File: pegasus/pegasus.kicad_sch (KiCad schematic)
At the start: 11 parts, among them IC1 L7805ACV, IC2 RFD900, IC3 L70B-M39, U1 Teensy4.0, U2 CON-SMA-EDGE-S, U3 CON-SMA-EDGE-S

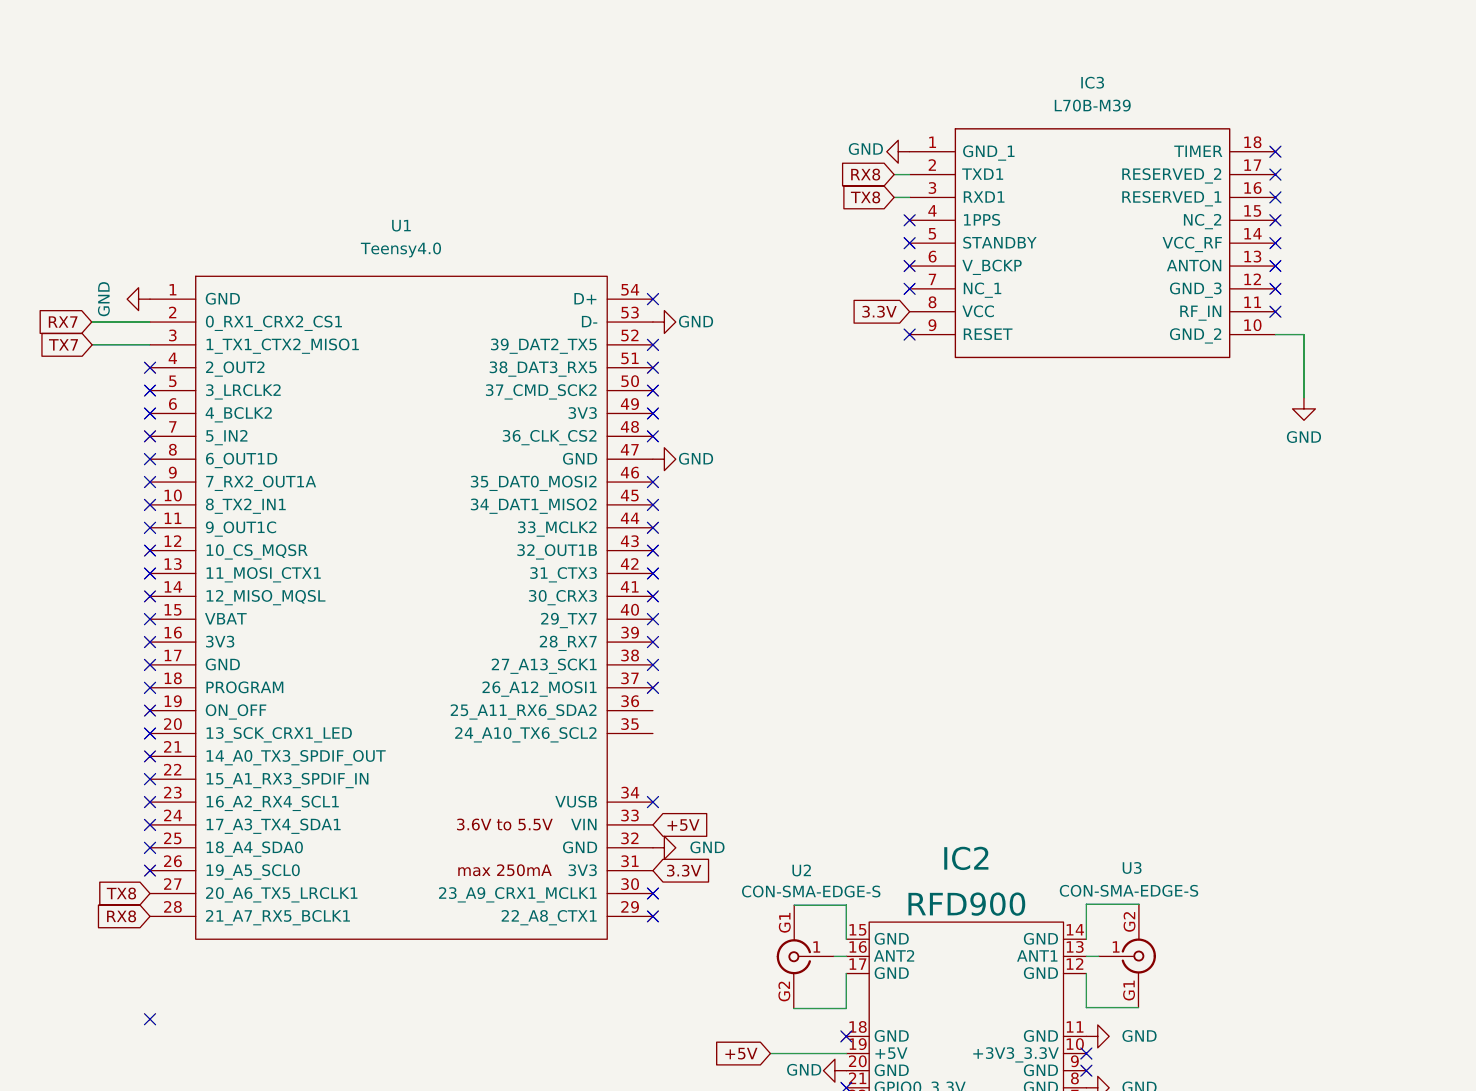
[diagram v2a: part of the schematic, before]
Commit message: add external RX TX connectors
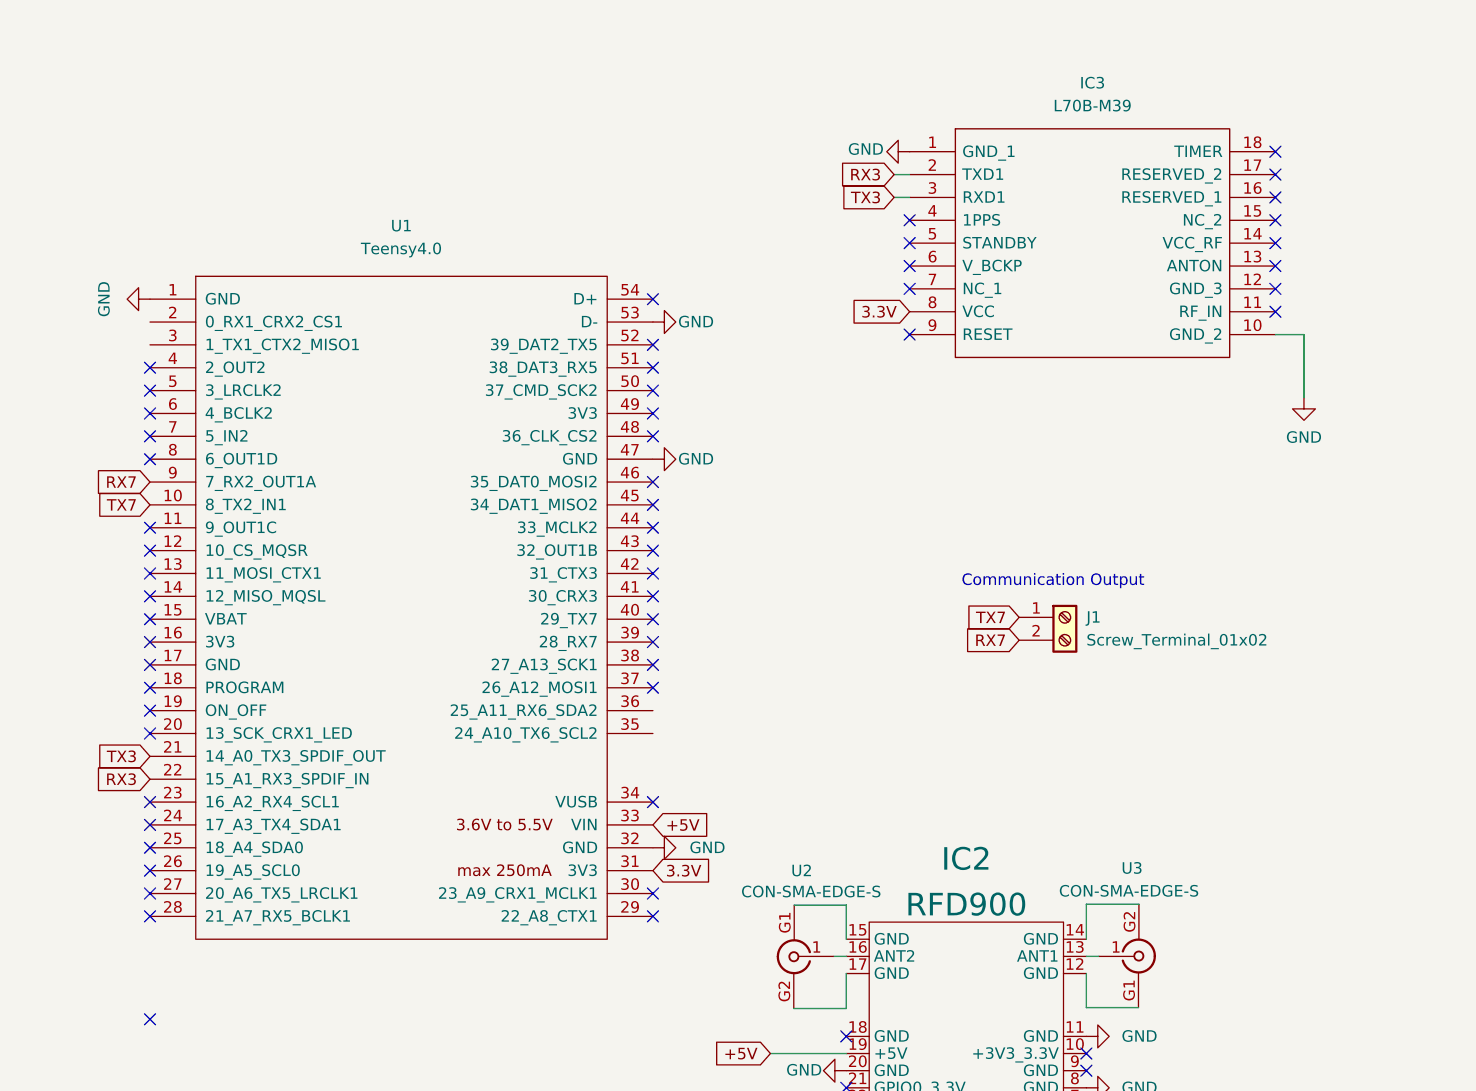
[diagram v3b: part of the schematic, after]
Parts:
- added J1: Screw_Terminal_01x02, RS-Components:SHDR2W105P0X500_1X2_1060X900X1250P, symbol Connector:Screw_Terminal_01x02
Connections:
- net RX7: now also U1.9 (7_RX2_OUT1A), J1.2 (Pin_2); no longer U1.2 (0_RX1_CRX2_CS1)
- net TX7: now also U1.10 (8_TX2_IN1), J1.1 (Pin_1); no longer U1.3 (1_TX1_CTX2_MISO1)
- net TX3: now reaches U1.21 (14_A0_TX3_SPDIF_OUT)
- net TX3: now also IC3.3 (RXD1)
- net RX3: now reaches U1.22 (15_A1_RX3_SPDIF_IN)
- net RX3: now also IC3.2 (TXD1)
- net RX8: no longer names the net of U1.28 (21_A7_RX5_BCLK1)
- net RX8: no longer IC3.2 (TXD1)
- net TX8: no longer names the net of U1.27 (20_A6_TX5_LRCLK1)
- net TX8: no longer IC3.3 (RXD1)
- no-connect marks 72 -> 70
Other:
- note added: "Communication Output"
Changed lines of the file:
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@@
   (no_connect (at 41.91 109.22))
   (no_connect (at 41.91 104.14))
-  (no_connect (at 41.91 111.76))
   (no_connect (at 41.91 106.68))
   (no_connect (at 41.91 101.6))
   (no_connect (at 41.91 99.06))
-  (no_connect (at 41.91 114.3))
   (no_connect (at 41.91 121.92))
   (no_connect (at 41.91 119.38))
@@
   (no_connect (at 41.91 139.7))
   (no_connect (at 41.91 171.45))
-  (no_connect (at 41.91 142.24))
+  (no_connect (at 41.91 147.32))
   (no_connect (at 41.91 154.94))
   (no_connect (at 41.91 149.86))
-  (no_connect (at 41.91 147.32))
-  (no_connect (at 41.91 144.78))
+  (no_connect (at 41.91 160.02))
+  (no_connect (at 41.91 157.48))
   (no_connect (at 145.9484 186.69))
   (no_connect (at 119.2784 192.405))
@@
     (stroke (width 0) (type default) (color 0 0 0 0))
   )
-  (wire (pts (xy 35.433 93.98) (xy 41.91 93.98))
-    (stroke (width 0) (type default) (color 0 0 0 0))
-  )
   (wire (pts (xy 56.134 34.544) (xy 56.134 42.164))
     (stroke (width 0) (type default) (color 0 0 0 0))
@@
     (stroke (width 0) (type default) (color 0 0 0 0))
   )
-  (wire (pts (xy 35.4838 96.52) (xy 41.91 96.52))
-    (stroke (width 0) (type default) (color 0 0 0 0))
-  )
   (wire (pts (xy 117.6528 188.595) (xy 119.2784 188.595))
     (stroke (width 0) (type default) (color 0 0 0 0))
@@
   (wire (pts (xy 145.9484 170.1546) (xy 145.9484 166.37))
     (stroke (width 0) (type default) (color 0 0 0 0))
+  )
+  (text "Communication Output\n" (at 132.08 123.5964 0)
+    (effects (font (size 1.27 1.27)) (justify left bottom))
   )
   (text "Switch\n" (at 38.1 37.846 90)
@@
     )
   )
-  (global_label "RX7" (shape input) (at 35.433 93.98 180) (fields_autoplaced)
-    (effects (font (size 1.27 1.27)) (justify right))
-    (property "Intersheet References" "${INTERSHEET_REFS}" (id 0) (at 29.3309 93.9006 0)
+  (global_label "RX7" (shape input) (at 41.91 111.76 180) (fields_autoplaced)
+    (effects (font (size 1.27 1.27)) (justify right))
+    (property "Intersheet References" "${INTERSHEET_REFS}" (id 0) (at 35.8079 111.6806 0)
       (effects (font (size 1.27 1.27)) (justify right) hide)
     )
@@
     )
   )
-  (global_label "RX8" (shape input) (at 41.91 160.02 180) (fields_autoplaced)
-    (effects (font (size 1.27 1.27)) (justify right))
-    (property "Intersheet References" "${INTERSHEET_REFS}" (id 0) (at 35.8079 160.0994 0)
+  (global_label "RX3" (shape input) (at 41.91 144.78 180) (fields_autoplaced)
+    (effects (font (size 1.27 1.27)) (justify right))
+    (property "Intersheet References" "${INTERSHEET_REFS}" (id 0) (at 35.8079 144.7006 0)
       (effects (font (size 1.27 1.27)) (justify right) hide)
     )
@@
     )
   )
-  (global_label "RX8" (shape input) (at 124.587 77.597 180) (fields_autoplaced)
-    (effects (font (size 1.27 1.27)) (justify right))
-    (property "Intersheet References" "${INTERSHEET_REFS}" (id 0) (at 118.4849 77.6764 0)
-      (effects (font (size 1.27 1.27)) (justify right) hide)
-    )
-  )
-  (global_label "TX8" (shape input) (at 124.587 80.137 180) (fields_autoplaced)
-    (effects (font (size 1.27 1.27)) (justify right))
-    (property "Intersheet References" "${INTERSHEET_REFS}" (id 0) (at 118.7872 80.2164 0)
+  (global_label "RX3" (shape input) (at 124.587 77.597 180) (fields_autoplaced)
+    (effects (font (size 1.27 1.27)) (justify right))
+    (property "Intersheet References" "${INTERSHEET_REFS}" (id 0) (at 118.4849 77.5176 0)
+      (effects (font (size 1.27 1.27)) (justify right) hide)
+    )
+  )
+  (global_label "TX3" (shape input) (at 124.587 80.137 180) (fields_autoplaced)
+    (effects (font (size 1.27 1.27)) (justify right))
+    (property "Intersheet References" "${INTERSHEET_REFS}" (id 0) (at 118.7872 80.0576 0)
+      (effects (font (size 1.27 1.27)) (justify right) hide)
+    )
+  )
+  (global_label "TX7" (shape input) (at 138.4808 126.7968 180) (fields_autoplaced)
+    (effects (font (size 1.27 1.27)) (justify right))
+    (property "Intersheet References" "${INTERSHEET_REFS}" (id 0) (at 132.681 126.7174 0)
       (effects (font (size 1.27 1.27)) (justify right) hide)
     )
@@
     )
   )
-  (global_label "TX8" (shape input) (at 41.91 157.48 180) (fields_autoplaced)
-    (effects (font (size 1.27 1.27)) (justify right))
-    (property "Intersheet References" "${INTERSHEET_REFS}" (id 0) (at 36.1102 157.5594 0)
+  (global_label "TX3" (shape input) (at 41.91 142.24 180) (fields_autoplaced)
+    (effects (font (size 1.27 1.27)) (justify right))
+    (property "Intersheet References" "${INTERSHEET_REFS}" (id 0) (at 36.1102 142.1606 0)
       (effects (font (size 1.27 1.27)) (justify right) hide)
     )
@@
     )
   )
-  (global_label "TX7" (shape input) (at 35.4838 96.52 180) (fields_autoplaced)
-    (effects (font (size 1.27 1.27)) (justify right))
-    (property "Intersheet References" "${INTERSHEET_REFS}" (id 0) (at 29.684 96.4406 0)
+  (global_label "RX7" (shape input) (at 138.4808 129.3368 180) (fields_autoplaced)
+    (effects (font (size 1.27 1.27)) (justify right))
+    (property "Intersheet References" "${INTERSHEET_REFS}" (id 0) (at 132.3787 129.2574 0)
+      (effects (font (size 1.27 1.27)) (justify right) hide)
+    )
+  )
+  (global_label "TX7" (shape input) (at 41.91 114.3 180) (fields_autoplaced)
+    (effects (font (size 1.27 1.27)) (justify right))
+    (property "Intersheet References" "${INTERSHEET_REFS}" (id 0) (at 36.1102 114.2206 0)
       (effects (font (size 1.27 1.27)) (justify right) hide)
     )
@@
   (symbol (lib_id "power:GND") (at 196.342 25.4 0) (unit 1)
     (in_bom yes) (on_board yes) (fields_autoplaced)
-    (property "Reference" "#PWR012" (id 0) (at 196.342 31.75 0)
+    (property "Reference" "#PWR011" (id 0) (at 196.342 31.75 0)
       (effects (font (size 1.27 1.27)) hide)
     )
@@
   (symbol (lib_id "power:GND") (at 214.376 25.908 0) (unit 1)
     (in_bom yes) (on_board yes) (fields_autoplaced)
-    (property "Reference" "#PWR013" (id 0) (at 214.376 32.258 0)
+    (property "Reference" "#PWR012" (id 0) (at 214.376 32.258 0)
       (effects (font (size 1.27 1.27)) hide)
     )
@@
   (symbol (lib_id "power:GND") (at 250.698 25.908 0) (unit 1)
     (in_bom yes) (on_board yes) (fields_autoplaced)
-    (property "Reference" "#PWR016" (id 0) (at 250.698 32.258 0)
+    (property "Reference" "#PWR014" (id 0) (at 250.698 32.258 0)
       (effects (font (size 1.27 1.27)) hide)
     )
@@
     )
     (pin "1")
+  )
+  (symbol (lib_id "Connector:Screw_Terminal_01x02") (at 143.5608 126.7968 0) (unit 1)
+    (in_bom yes) (on_board yes) (fields_autoplaced)
+    (property "Reference" "J1" (id 0) (at 145.9484 126.7967 0)
+      (effects (font (size 1.27 1.27)) (justify left))
+    )
+    (property "Value" "Screw_Terminal_01x02" (id 1) (at 145.9484 129.3367 0)
+      (effects (font (size 1.27 1.27)) (justify left))
+    )
+    (property "Footprint" "RS-Components:SHDR2W105P0X500_1X2_1060X900X1250P" (id 2) (at 143.5608 126.7968 0)
+      (effects (font (size 1.27 1.27)) hide)
+    )
+    (property "Datasheet" "~" (id 3) (at 143.5608 126.7968 0)
+      (effects (font (size 1.27 1.27)) hide)
+    )
+    (pin "1")
+    (pin "2")
   )
   (symbol (lib_id "Quectel_L70B-M39:L70B-M39") (at 126.3142 75.057 0) (unit 1)
@@
   (symbol (lib_id "power:GND") (at 232.664 25.908 0) (unit 1)
     (in_bom yes) (on_board yes) (fields_autoplaced)
-    (property "Reference" "#PWR015" (id 0) (at 232.664 32.258 0)
+    (property "Reference" "#PWR013" (id 0) (at 232.664 32.258 0)
       (effects (font (size 1.27 1.27)) hide)
     )
@@
     )
     (path "/70e52f12-fb67-4276-ad30-28892fb20b86"
+      (reference "#PWR011") (unit 1) (value "GND") (footprint "")
+    )
+    (path "/78a4a849-1c24-4beb-98bb-5d8b5b1babf4"
       (reference "#PWR012") (unit 1) (value "GND") (footprint "")
     )
-    (path "/78a4a849-1c24-4beb-98bb-5d8b5b1babf4"
+    (path "/c629176b-abd3-4695-ae9b-e765a0bc8aed"
       (reference "#PWR013") (unit 1) (value "GND") (footprint "")
     )
-    (path "/c629176b-abd3-4695-ae9b-e765a0bc8aed"
-      (reference "#PWR015") (unit 1) (value "GND") (footprint "")
-    )
     (path "/abaa90e7-ead3-4e66-bb3e-cc1d7a6daa0e"
-      (reference "#PWR016") (unit 1) (value "GND") (footprint "")
+      (reference "#PWR014") (unit 1) (value "GND") (footprint "")
     )
     (path "/fa097515-aa33-445e-a81c-63a2092f37d7"
@@
       (reference "IC3") (unit 1) (value "L70B-M39") (footprint "Quectel_L70B-M39:1x18")
     )
+    (path "/bb9478d8-9393-4633-8eab-e3cdf1c5ff7e"
+      (reference "J1") (unit 1) (value "Screw_Terminal_01x02") (footprint "RS-Components:SHDR2W105P0X500_1X2_1060X900X1250P")
+    )
     (path "/d4822f5d-8c1d-4b0c-ba23-0826fc0572d8"

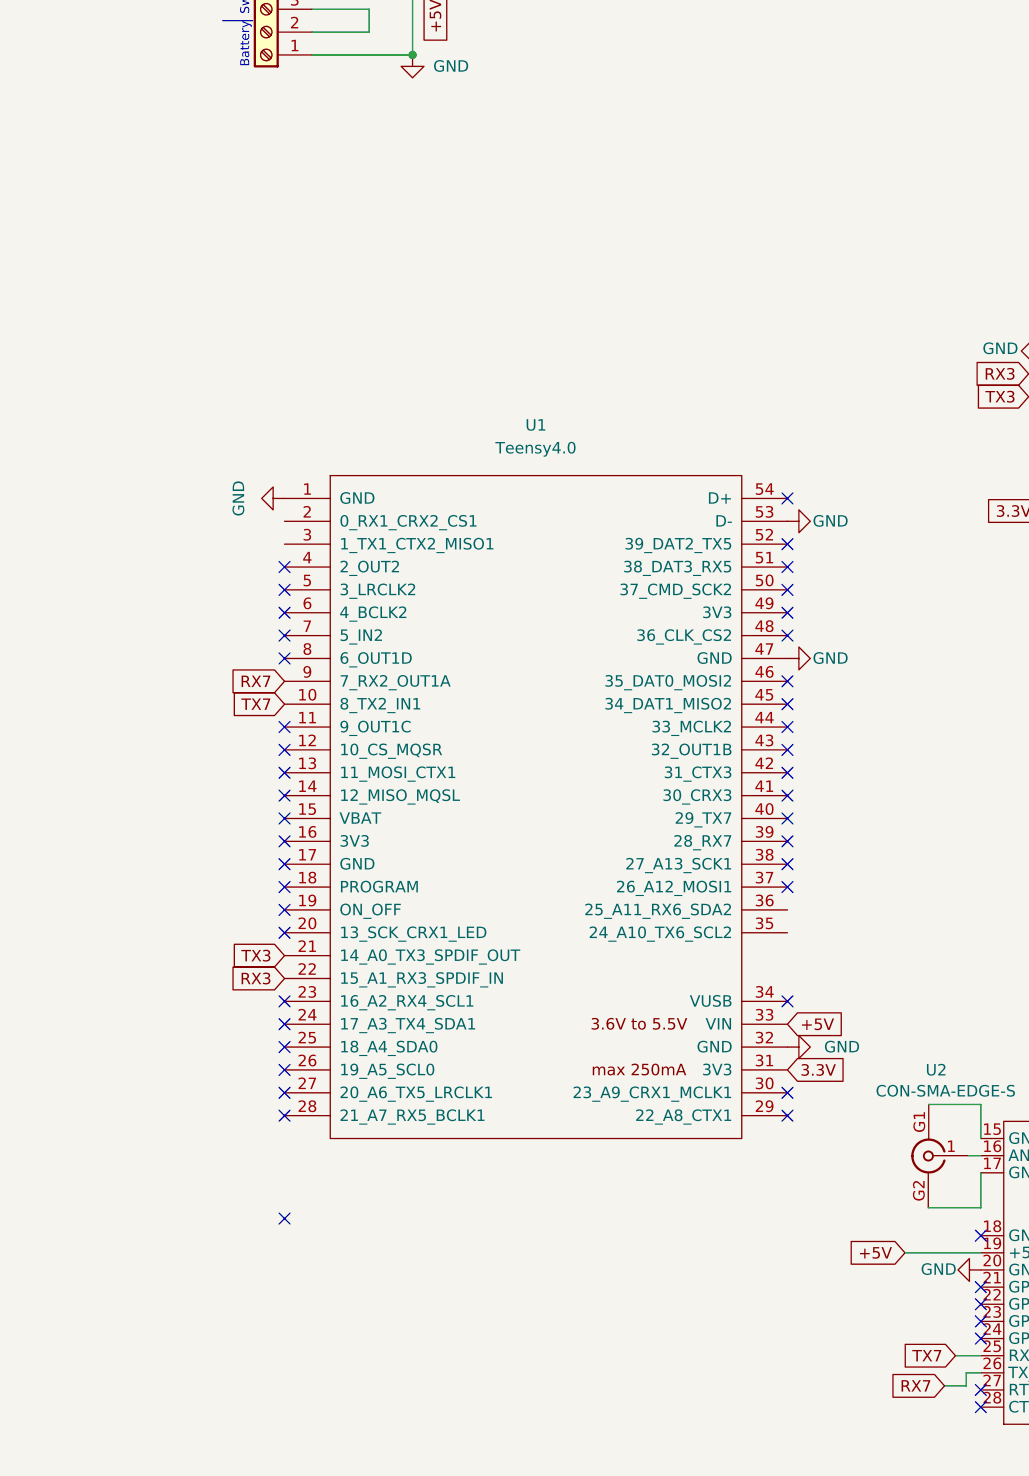
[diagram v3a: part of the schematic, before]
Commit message: add rgb led
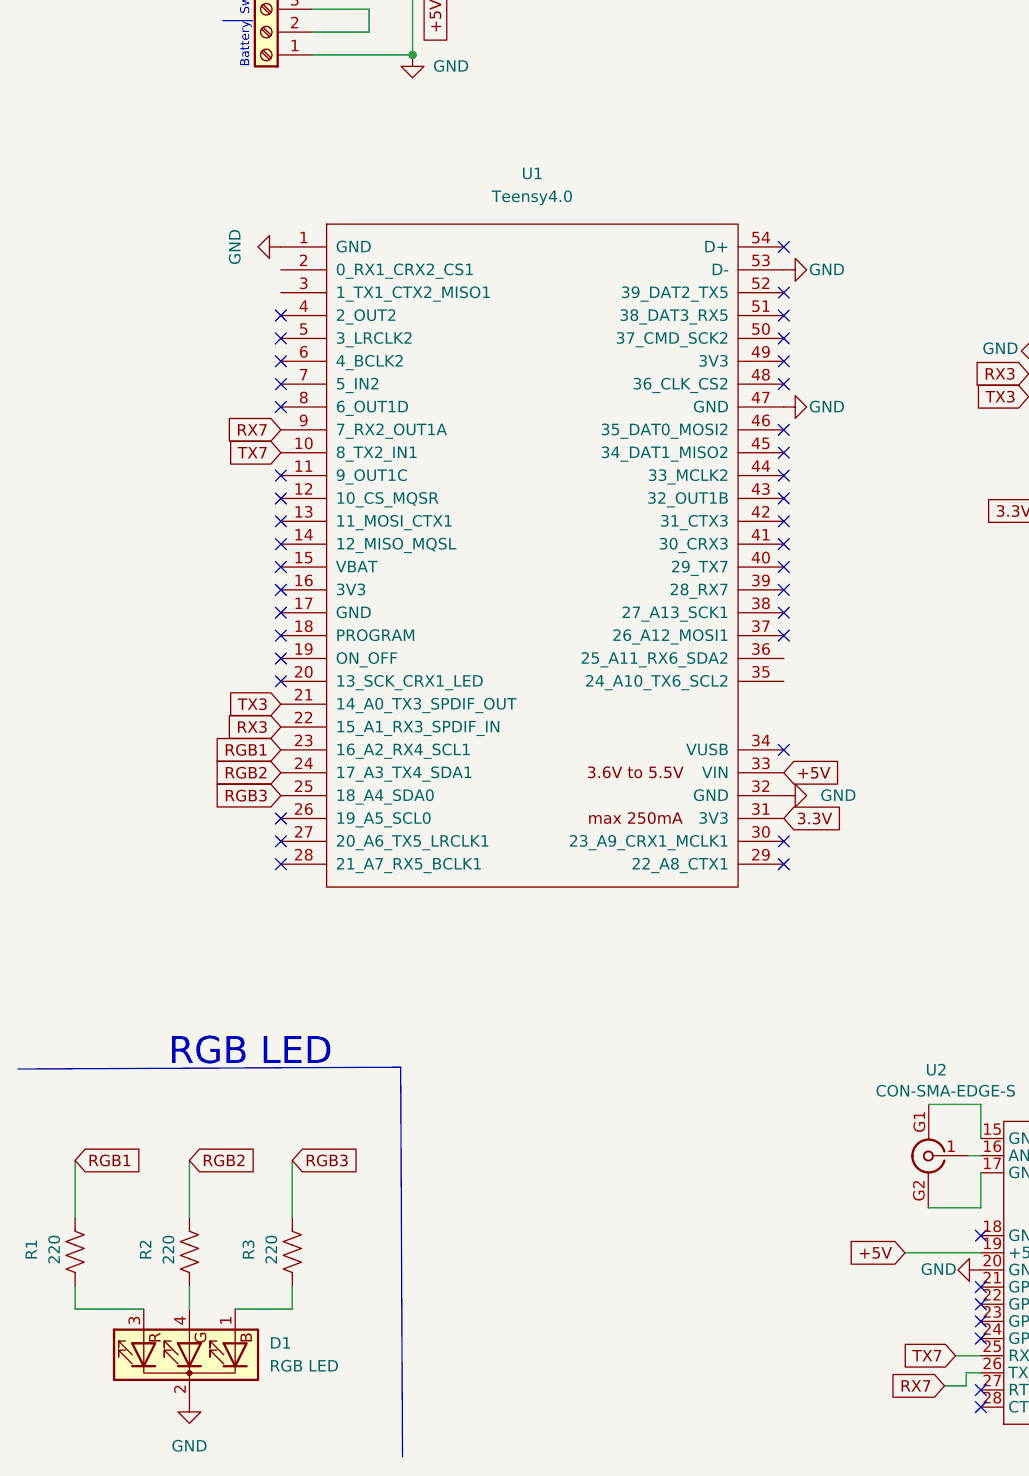
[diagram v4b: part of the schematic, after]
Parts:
- added D1: RGB LED, LED_THT:LED_D5.0mm-4_RGB, symbol Device:LED_BKRG
- added R1, R2, R3: 220, Resistor_SMD:R_1206_3216Metric_Pad1.30x1.75mm_HandSolder, symbol Device:R_US
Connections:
- net GND: now also D1.2 (K)
- net RGB1: now reaches U1.23 (16_A2_RX4_SCL1)
- net RGB1: now also R1.2
- net RGB2: now reaches U1.24 (17_A3_TX4_SDA1)
- net RGB2: now also R2.2
- net RGB3: now reaches U1.25 (18_A4_SDA0)
- net RGB3: now also R3.2
- new net: D1.3 (RA), R1.1
- new net: D1.4 (GA), R2.1
- new net: D1.1 (BA), R3.1
- no-connect marks 70 -> 66
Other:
- note added: "RGB LED"
- moved on the sheet: U1
